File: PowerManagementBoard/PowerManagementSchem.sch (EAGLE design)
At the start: 122 parts, among them J1 D15S24A4GV00LF, J8 182-037-213R531, J9 182-025-213R531, Q1 PMOSFET, Q10 PMOSFET, Q11 PMOSFET, Q12 PMOSFET, Q2 PMOSFET, Q3 PMOSFET, Q4 PMOSFET, Q5 PMOSFET, Q6 PMOSFET, Q7 PMOSFET, Q8 PMOSFET, Q9 PMOSFET, U1 VX7805-500, U2 PYB20-Q24-S5, U3 PYB30-Q48-S5, U4 PYB30-Q48-S12, U5 3V3REG, U6 INA4180-SPLIT, U7 INA4180-SPLIT, U8 TEENSY-4.0SILK, U9 INA4180-SPLIT

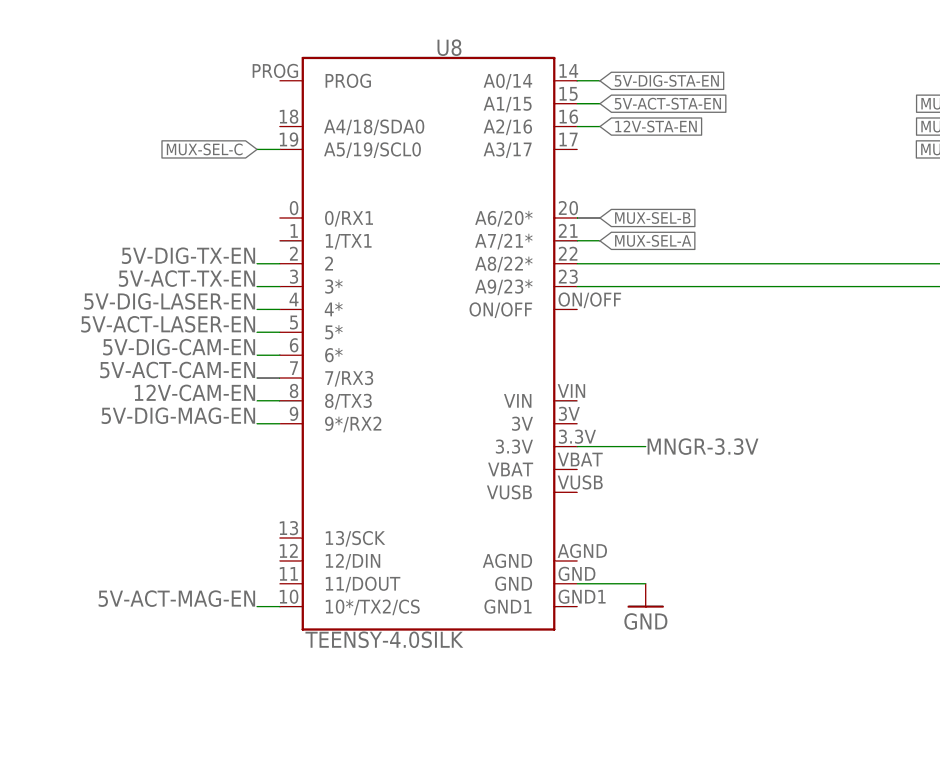
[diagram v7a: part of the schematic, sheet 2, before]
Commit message: Completed routing of power board. Ready for checking.
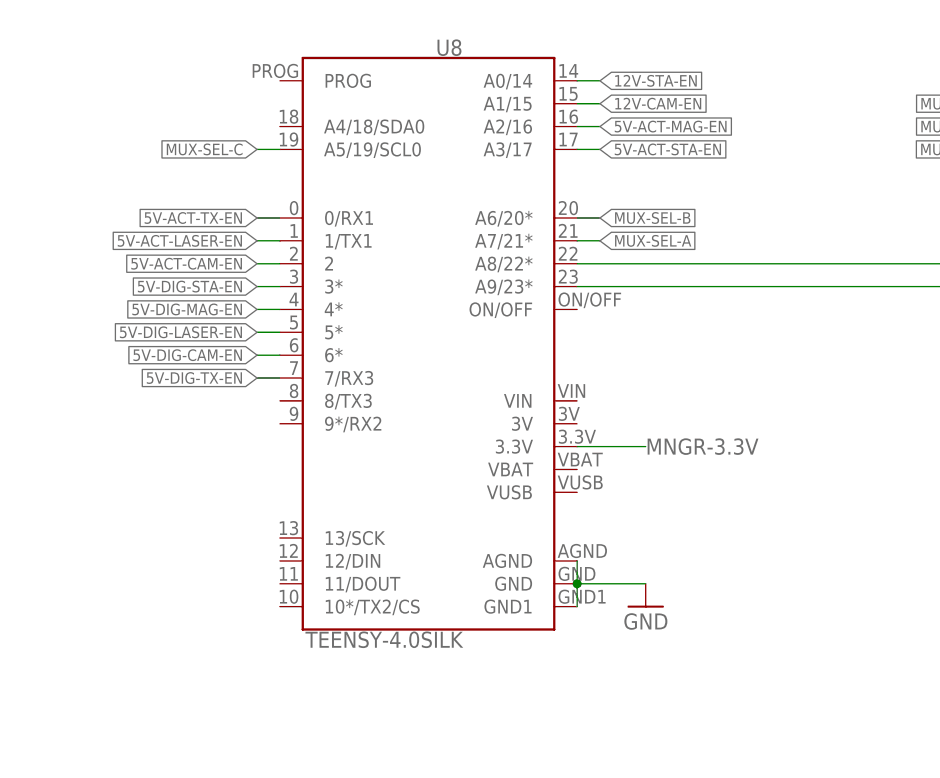
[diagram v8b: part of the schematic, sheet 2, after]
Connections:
- removed net N$37: J3.20
- net 12V-CAM-EN: now also U8.A1/15; no longer U8.8/TX3
- net 12V-STA-EN: now also U8.A0/14; no longer U8.A2/16
- net 5V-ACT-CAM-EN: now also U8.2; no longer U8.7/RX3
- net 5V-ACT-LASER-EN: now also U8.1/TX1; no longer U8.5*
- net 5V-ACT-MAG-EN: now also U8.A2/16; no longer U8.10*/TX2/CS
- net 5V-ACT-STA-EN: now also U8.A3/17; no longer U8.A1/15
- net 5V-ACT-TX-EN: now also U8.0/RX1; no longer U8.3*
- net 5V-DIG-LASER-EN: now also U8.5*; no longer U8.4*
- net 5V-DIG-MAG-EN: now also U8.4*; no longer U8.9*/RX2
- net 5V-DIG-STA-EN: now also U8.3*; no longer U8.A0/14
- net 5V-DIG-TX-EN: now also U8.7/RX3; no longer U8.2
- net GND: now also U8.AGND, U8.GND1
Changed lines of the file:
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@@
 <pinref part="GND19" gate="1" pin="GND"/>
 <wire x1="83.82" y1="106.68" x2="91.44" y2="106.68" width="0.1524" layer="91"/>
+<pinref part="U8" gate="G$1" pin="GND1"/>
+<wire x1="83.82" y1="104.14" x2="83.82" y2="106.68" width="0.1524" layer="91"/>
+<junction x="83.82" y="106.68"/>
+<pinref part="U8" gate="G$1" pin="AGND"/>
+<wire x1="83.82" y1="109.22" x2="83.82" y2="106.68" width="0.1524" layer="91"/>
 </segment>
 <segment>
@@
 <wire x1="175.26" y1="99.06" x2="172.72" y2="99.06" width="0.1524" layer="91"/>
 <junction x="175.26" y="99.06"/>
-</segment>
-</net>
-<net name="5V-DIG-TX-EN" class="0">
-<segment>
-<pinref part="U8" gate="G$1" pin="2"/>
-<wire x1="50.8" y1="142.24" x2="48.26" y2="142.24" width="0.1524" layer="91"/>
-<label x="48.26" y="142.24" size="1.778" layer="95" rot="MR0"/>
-</segment>
-</net>
-<net name="5V-ACT-TX-EN" class="0">
-<segment>
-<pinref part="U8" gate="G$1" pin="3*"/>
-<wire x1="50.8" y1="139.7" x2="48.26" y2="139.7" width="0.1524" layer="91"/>
-<label x="48.26" y="139.7" size="1.778" layer="95" rot="MR0"/>
-</segment>
-</net>
-<net name="5V-DIG-LASER-EN" class="0">
-<segment>
-<pinref part="U8" gate="G$1" pin="4*"/>
-<wire x1="50.8" y1="137.16" x2="48.26" y2="137.16" width="0.1524" layer="91"/>
-<label x="48.26" y="137.16" size="1.778" layer="95" rot="MR0"/>
-</segment>
-</net>
-<net name="5V-ACT-LASER-EN" class="0">
-<segment>
-<pinref part="U8" gate="G$1" pin="5*"/>
-<wire x1="50.8" y1="134.62" x2="48.26" y2="134.62" width="0.1524" layer="91"/>
-<label x="48.26" y="134.62" size="1.778" layer="95" rot="MR0"/>
-</segment>
-</net>
-<net name="5V-DIG-CAM-EN" class="0">
-<segment>
-<pinref part="U8" gate="G$1" pin="6*"/>
-<wire x1="50.8" y1="132.08" x2="48.26" y2="132.08" width="0.1524" layer="91"/>
-<label x="48.26" y="132.08" size="1.778" layer="95" rot="MR0"/>
-</segment>
-</net>
-<net name="5V-ACT-CAM-EN" class="0">
-<segment>
-<pinref part="U8" gate="G$1" pin="7/RX3"/>
-<wire x1="50.8" y1="129.54" x2="48.26" y2="129.54" width="0.1524" layer="91"/>
-<label x="48.26" y="129.54" size="1.778" layer="95" rot="MR0"/>
-</segment>
-</net>
-<net name="12V-CAM-EN" class="0">
-<segment>
-<pinref part="U8" gate="G$1" pin="8/TX3"/>
-<wire x1="50.8" y1="127" x2="48.26" y2="127" width="0.1524" layer="91"/>
-<label x="48.26" y="127" size="1.778" layer="95" rot="MR0"/>
-</segment>
-</net>
-<net name="5V-DIG-MAG-EN" class="0">
-<segment>
-<pinref part="U8" gate="G$1" pin="9*/RX2"/>
-<wire x1="50.8" y1="124.46" x2="48.26" y2="124.46" width="0.1524" layer="91"/>
-<label x="48.26" y="124.46" size="1.778" layer="95" rot="MR0"/>
-</segment>
-</net>
-<net name="5V-ACT-MAG-EN" class="0">
-<segment>
-<pinref part="U8" gate="G$1" pin="10*/TX2/CS"/>
-<wire x1="50.8" y1="104.14" x2="48.26" y2="104.14" width="0.1524" layer="91"/>
-<label x="48.26" y="104.14" size="1.778" layer="95" rot="MR0"/>
 </segment>
 </net>
@@
 </segment>
 </net>
+<net name="5V-ACT-TX-EN" class="0">
+<segment>
+<pinref part="U8" gate="G$1" pin="0/RX1"/>
+<wire x1="50.8" y1="147.32" x2="48.26" y2="147.32" width="0.1524" layer="91"/>
+<label x="48.26" y="147.32" size="1.27" layer="95" rot="R180" xref="yes"/>
+</segment>
+</net>
+<net name="5V-ACT-LASER-EN" class="0">
+<segment>
+<pinref part="U8" gate="G$1" pin="1/TX1"/>
+<wire x1="50.8" y1="144.78" x2="48.26" y2="144.78" width="0.1524" layer="91"/>
+<label x="48.26" y="144.78" size="1.27" layer="95" rot="R180" xref="yes"/>
+</segment>
+</net>
+<net name="5V-ACT-CAM-EN" class="0">
+<segment>
+<pinref part="U8" gate="G$1" pin="2"/>
+<wire x1="50.8" y1="142.24" x2="48.26" y2="142.24" width="0.1524" layer="91"/>
+<label x="48.26" y="142.24" size="1.27" layer="95" rot="R180" xref="yes"/>
+</segment>
+</net>
 <net name="5V-DIG-STA-EN" class="0">
 <segment>
-<pinref part="U8" gate="G$1" pin="A0/14"/>
-<wire x1="86.36" y1="162.56" x2="83.82" y2="162.56" width="0.1524" layer="91"/>
-<label x="86.36" y="162.56" size="1.27" layer="95" xref="yes"/>
+<pinref part="U8" gate="G$1" pin="3*"/>
+<wire x1="50.8" y1="139.7" x2="48.26" y2="139.7" width="0.1524" layer="91"/>
+<label x="48.26" y="139.7" size="1.27" layer="95" rot="R180" xref="yes"/>
+</segment>
+</net>
+<net name="5V-DIG-MAG-EN" class="0">
+<segment>
+<pinref part="U8" gate="G$1" pin="4*"/>
+<wire x1="50.8" y1="137.16" x2="48.26" y2="137.16" width="0.1524" layer="91"/>
+<label x="48.26" y="137.16" size="1.27" layer="95" rot="R180" xref="yes"/>
+</segment>
+</net>
+<net name="5V-DIG-LASER-EN" class="0">
+<segment>
+<pinref part="U8" gate="G$1" pin="5*"/>
+<wire x1="50.8" y1="134.62" x2="48.26" y2="134.62" width="0.1524" layer="91"/>
+<label x="48.26" y="134.62" size="1.27" layer="95" rot="R180" xref="yes"/>
+</segment>
+</net>
+<net name="5V-DIG-CAM-EN" class="0">
+<segment>
+<pinref part="U8" gate="G$1" pin="6*"/>
+<wire x1="50.8" y1="132.08" x2="48.26" y2="132.08" width="0.1524" layer="91"/>
+<label x="48.26" y="132.08" size="1.27" layer="95" rot="R180" xref="yes"/>
+</segment>
+</net>
+<net name="5V-DIG-TX-EN" class="0">
+<segment>
+<pinref part="U8" gate="G$1" pin="7/RX3"/>
+<wire x1="50.8" y1="129.54" x2="48.26" y2="129.54" width="0.1524" layer="91"/>
+<label x="48.26" y="129.54" size="1.27" layer="95" rot="R180" xref="yes"/>
 </segment>
 </net>
 <net name="5V-ACT-STA-EN" class="0">
+<segment>
+<pinref part="U8" gate="G$1" pin="A3/17"/>
+<wire x1="83.82" y1="154.94" x2="86.36" y2="154.94" width="0.1524" layer="91"/>
+<label x="86.36" y="154.94" size="1.27" layer="95" xref="yes"/>
+</segment>
+</net>
+<net name="5V-ACT-MAG-EN" class="0">
+<segment>
+<pinref part="U8" gate="G$1" pin="A2/16"/>
+<wire x1="83.82" y1="157.48" x2="86.36" y2="157.48" width="0.1524" layer="91"/>
+<label x="86.36" y="157.48" size="1.27" layer="95" xref="yes"/>
+</segment>
+</net>
+<net name="12V-CAM-EN" class="0">
 <segment>
 <pinref part="U8" gate="G$1" pin="A1/15"/>
@@
 <net name="12V-STA-EN" class="0">
 <segment>
-<pinref part="U8" gate="G$1" pin="A2/16"/>
-<wire x1="83.82" y1="157.48" x2="86.36" y2="157.48" width="0.1524" layer="91"/>
-<label x="86.36" y="157.48" size="1.27" layer="95" xref="yes"/>
+<pinref part="U8" gate="G$1" pin="A0/14"/>
+<wire x1="83.82" y1="162.56" x2="86.36" y2="162.56" width="0.1524" layer="91"/>
+<label x="86.36" y="162.56" size="1.27" layer="95" xref="yes"/>
 </segment>
 </net>
@@
 </segment>
 </net>
-<net name="N$37" class="0">
-<segment>
-<pinref part="J3" gate="G$1" pin="20"/>
-<wire x1="111.76" y1="10.16" x2="114.3" y2="10.16" width="0.1524" layer="91"/>
-</segment>
-</net>
 <net name="ANT-MOSI_2" class="0">
 <segment>
@@
 </sheet>
 </sheets>
+<errors>
+</errors>
 </schematic>
 </drawing>
